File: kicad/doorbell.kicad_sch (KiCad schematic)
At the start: 94 parts, among them J1 USB-C (USB4105), J2 WF26 bus, K1 GAQW212GS, K2 GAQY212GS, K3 GAQY412EH, K4 GAQY412EH, K5 G6K-2F-Y DC12, Q3 2N7002, Q4 2N7002, SW1 BOOT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

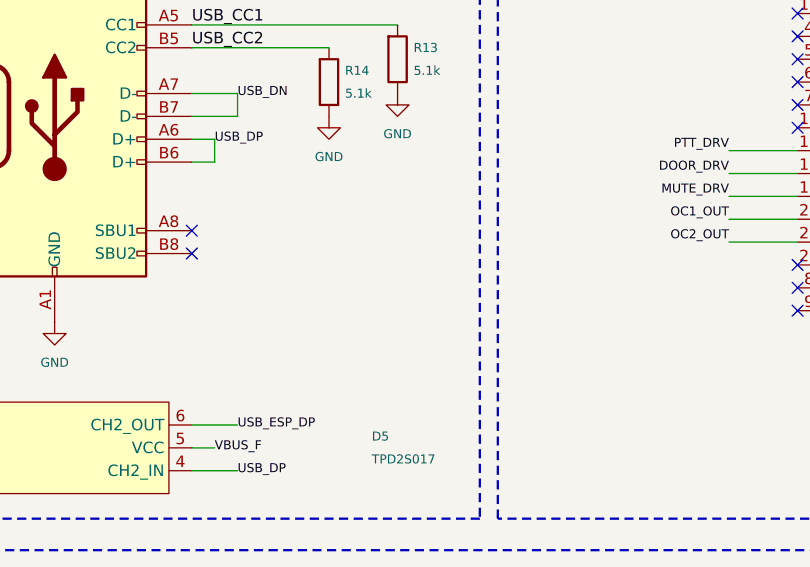
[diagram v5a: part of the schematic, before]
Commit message: kicad+sim: dedicated LP5907 AVDD LDO + J3 USB wall-feed connector
kicad:
- AVDD now comes from a dedicated low-noise LDO (U4 = LP5907MFX-3.3) off +5V:
  AU_3V3 -> FB1 -> AVDD, isolating the codec analog rail from the Wi-Fi/SMPS-noisy
  +3V3 plane (C23/C24 in/out caps; EN tied to +3V3 for sequencing).
- Add J3 -- JST-SH side-entry wall-feed connector (power + native USB); D+/D-
  routed as a pair on B.Cu to the D5/J1 connector-side hub (shares D5's ESD clamp).
- Sourcing fields (LCSC/MPN/Manufacturer) + role Descriptions for U4 and J3;
  correct FB1's role (second LC pole on AU_3V3, no longer "isolates from +3V3").

sim:
- Model the LP5907 as an LDO (Ldo recognises bare IN/OUT pins, not just VIN/VOUT;
  per-part VIN abs-max -- 6 V for the LP5907 vs 22 V for the SGM2212) and register
  it in the model-coverage gate.
- RX tests now drive only the external VBUS, so AVDD comes up through the new LDO.

TODO: defer VBUS source isolation between J1 (USB-C) and J3 (wall feed) --
TPS2116 power-mux or a two-diode front-OR; no board room for it now.
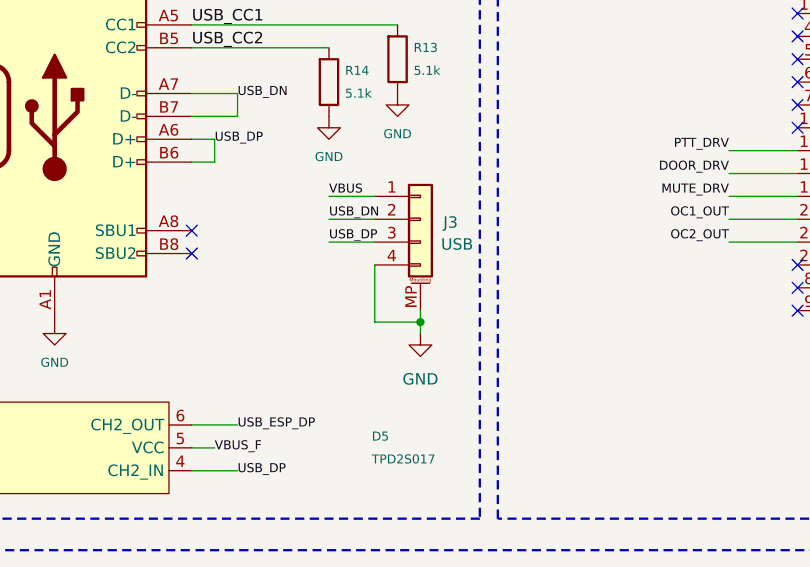
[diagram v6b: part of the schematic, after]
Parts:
- added J3: USB, Connector_JST:JST_SH_SM04B-SRSS-TB_1x04-1MP_P1.00mm_Horizontal, symbol Connector_Generic_MountingPin:Conn_01x04_MountingPin
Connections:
- net GND: now also J3.4 (Pin_4), J3.MP (MountPin)
- net USB_DN: now also J3.2 (Pin_2)
- net USB_DP: now also J3.3 (Pin_3)
- net VBUS: now also J3.1 (Pin_1)

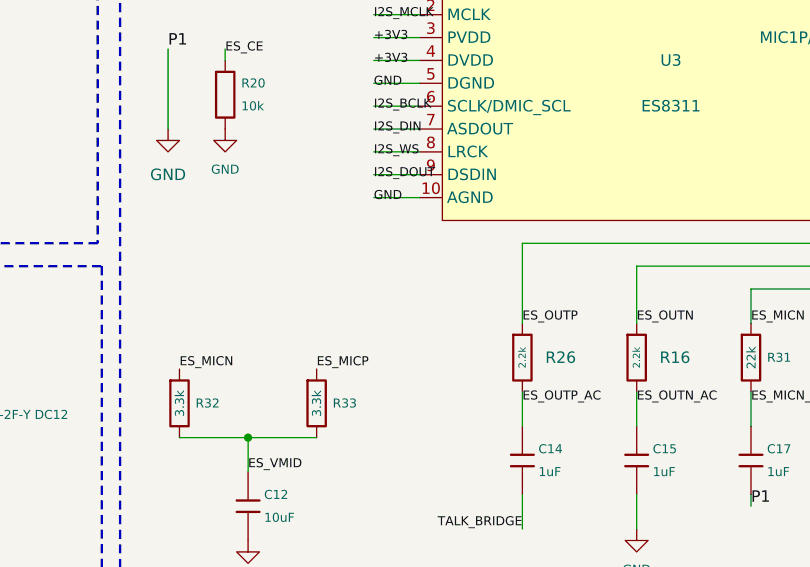
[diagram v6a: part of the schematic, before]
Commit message: codec OUTP clamp (D13 BAT54S) + sim model + doc sync
Add the BAT54S dual-series Schottky clamp at the ES8311 OUTP (D13: COM -> ES_OUTP,
A -> GND, K -> +3V3) as the OUTP abs-max guard. R26 limits the current into it, so the
clamp holds OUTP within [AGND-0.3, AVDD+0.3] against both the per-talk-start K1-make
transient and a single-fault C14-short, instead of leaning on the codec's unrated
internal ESD diode. Board placed + routed, zones refilled, DRC clean.

- sim: DiodeArray model for the 3-pin series array (Diode only handles 2-terminal
  parts) + reviewed model-coverage entry; 50/50 tests pass
- DESIGN.md: TX front-end note -> "R26 + D13 form the OUTP abs-max guard"
- REQUIREMENTS.md: AUDIO-9 (TX/OUTP abs-max, counterpart to AUDIO-8)
- TODO.md: drop completed items (OUTP clamp, SW4 PTT fit, D5 refdes)
- remove stale scratch docs (CODEC_AVDD_REWORK.md, JLCPCB-BASIC-PARTS.md)
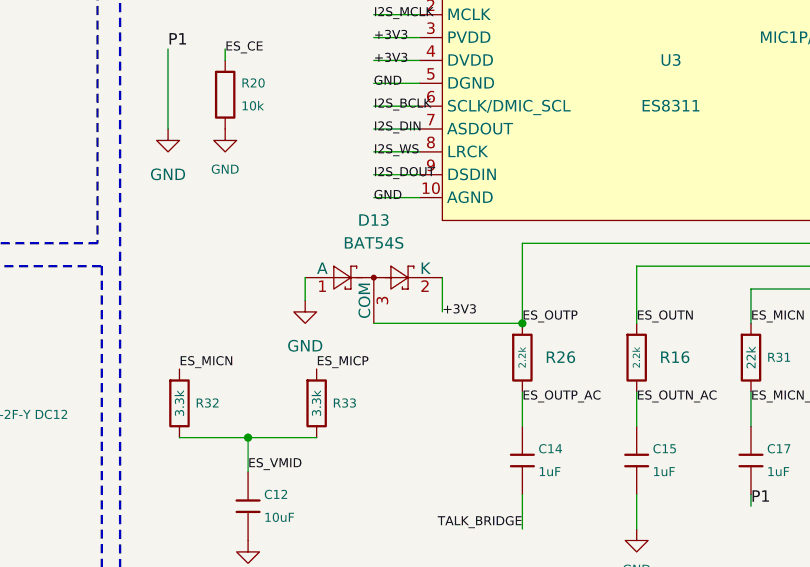
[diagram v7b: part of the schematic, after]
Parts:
- added D13: BAT54S, Package_TO_SOT_SMD:SOT-23, symbol Diode:BAT54S
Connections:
- net +3V3: now also D13.2 (K)
- net ES_OUTP: now also D13.3 (COM)
- net GND: now also D13.1 (A)
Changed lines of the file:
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@@
 	)
 	(junction
+		(at 203.2 217.17)
+		(diameter 0)
+		(color 0 0 0 0)
+	)
+	(junction
 		(at 226.06 29.21)
 		(diameter 0)
@@
 	(wire
 		(pts
+			(xy 186.69 217.17) (xy 203.2 217.17)
+		)
+		(stroke
+			(width 0)
+			(type default)
+		)
+	)
+	(wire
+		(pts
 			(xy 63.5 85.09) (xy 68.58 85.09)
 		)
@@
 	(wire
 		(pts
+			(xy 179.07 212.09) (xy 179.07 214.63)
+		)
+		(stroke
+			(width 0)
+			(type default)
+		)
+	)
+	(wire
+		(pts
 			(xy 43.18 138.43) (xy 49.53 138.43)
 		)
@@
 	(wire
 		(pts
+			(xy 194.31 212.09) (xy 194.31 215.9)
+		)
+		(stroke
+			(width 0)
+			(type default)
+		)
+	)
+	(wire
+		(pts
 			(xy 22.86 251.46) (xy 50.8 251.46)
 		)
@@
 		)
 	)
+	(label "+3V3"
+		(at 194.31 215.9 0)
+		(effects
+			(font
+				(size 1 1)
+			)
+			(justify left)
+		)
+	)
 	(label "DOOR_DRV"
 		(at 285.75 180.34 180)
@@
 			)
 		)
-    (property "LCSC" "C160404" (at 88.9 62.23 0)
-      (effects (font (size 1.27 1.27)) (hide yes))
-    )
-    (property "MPN" "SM04B-SRSS-TB(LF)(SN)" (at 88.9 62.23 0)
-      (effects (font (size 1.27 1.27)) (hide yes))
-    )
-    (property "Manufacturer" "JST" (at 88.9 62.23 0)
-      (effects (font (size 1.27 1.27)) (hide yes))
-    )
+		(property "LCSC" "C160404"
+			(at 88.9 62.23 0)
+			(hide yes)
+			(show_name no)
+			(do_not_autoplace no)
+			(effects
+				(font
+					(size 1.27 1.27)
+				)
+			)
+		)
+		(property "MPN" "SM04B-SRSS-TB(LF)(SN)"
+			(at 88.9 62.23 0)
+			(hide yes)
+			(show_name no)
+			(do_not_autoplace no)
+			(effects
+				(font
+					(size 1.27 1.27)
+				)
+			)
+		)
+		(property "Manufacturer" "JST"
+			(at 88.9 62.23 0)
+			(hide yes)
+			(show_name no)
+			(do_not_autoplace no)
+			(effects
+				(font
+					(size 1.27 1.27)
+				)
+			)
+		)
 		(pin "1"
 		)
@@
 	)
 	(symbol
+		(lib_id "power:GND")
+		(at 179.07 214.63 0)
+		(unit 1)
+		(body_style 1)
+		(exclude_from_sim no)
+		(in_bom yes)
+		(on_board yes)
+		(in_pos_files yes)
+		(dnp no)
+		(fields_autoplaced yes)
+		(property "Reference" "#PWR059"
+			(at 179.07 220.98 0)
+			(hide yes)
+			(show_name no)
+			(do_not_autoplace no)
+			(effects
+				(font
+					(size 1.27 1.27)
+				)
+			)
+		)
+		(property "Value" "GND"
+			(at 179.07 219.71 0)
+			(show_name no)
+			(do_not_autoplace no)
+			(effects
+				(font
+					(size 1.27 1.27)
+				)
+			)
+		)
+		(property "Footprint" ""
+			(at 179.07 214.63 0)
+			(hide yes)
+			(show_name no)
+			(do_not_autoplace no)
+			(effects
+				(font
+					(size 1.27 1.27)
+				)
+			)
+		)
+		(property "Datasheet" ""
+			(at 179.07 214.63 0)
+			(hide yes)
+			(show_name no)
+			(do_not_autoplace no)
+			(effects
+				(font
+					(size 1.27 1.27)
+				)
+			)
+		)
+		(property "Description" "Power symbol creates a global label with name \"GND\" , ground"
+			(at 179.07 214.63 0)
+			(hide yes)
+			(show_name no)
+			(do_not_autoplace no)
+			(effects
+				(font
+					(size 1.27 1.27)
+				)
+			)
+		)
+		(pin "1"
+		)
+		(instances
+			(project "doorbell"
+				(path "/959c5810-086a-4a51-98b0-f68b22907a4f"
+					(reference "#PWR059")
+					(unit 1)
+				)
+			)
+		)
+	)
+	(symbol
 		(lib_id "power:+3V3")
 		(at 146.05 20.32 0)
@@
 					(unit 1)
 				)
+			)
+		)
+	)
+	(symbol
+		(lib_id "Diode:BAT54S")
+		(at 186.69 212.09 0)
+		(unit 1)
+		(body_style 1)
+		(exclude_from_sim no)
+		(in_bom yes)
+		(on_board yes)
+		(in_pos_files yes)
+		(dnp no)
+		(fields_autoplaced yes)
+		(property "Reference" "D13"
+			(at 186.69 205.74 0)
+			(show_name no)
+			(do_not_autoplace no)
+			(effects
+				(font
+					(size 1.27 1.27)
+				)
+			)
+		)
+		(property "Value" "BAT54S"
+			(at 186.69 208.28 0)
+			(show_name no)
+			(do_not_autoplace no)
+			(effects
+				(font
+					(size 1.27 1.27)
+				)
+			)
+		)
+		(property "Footprint" "Package_TO_SOT_SMD:SOT-23"
+			(at 188.595 208.915 0)
+			(hide yes)
+			(show_name no)
+			(do_not_autoplace no)
+			(effects
+				(font
+					(size 1.27 1.27)
+				)
+				(justify left)
+			)
+		)
+		(property "Datasheet" "https://www.diodes.com/assets/Datasheets/ds11005.pdf"
+			(at 183.642 212.09 0)
+			(hide yes)
+			(show_name no)
+			(do_not_autoplace no)
+			(effects
+				(font
+					(size 1.27 1.27)
+				)
+			)
+		)
+		(property "Description" "Vr 30V, If 200mA, Dual schottky barrier diode, in series, SOT-323"
+			(at 186.69 212.09 0)
+			(hide yes)
+			(show_name no)
+			(do_not_autoplace no)
+			(effects
+				(font
+					(size 1.27 1.27)
+				)
+			)
+		)
+		(pin "1"
+		)
+		(pin "2"
+		)
+		(pin "3"
+		)
+		(instances
+			(project "doorbell"
+				(path "/959c5810-086a-4a51-98b0-f68b22907a4f"
+					(reference "D13")
+					(unit 1)
+				)

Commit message: docs + BOM sourcing: D13 LCSC, full datasheet set, MCU/vendor doc fixes
Completes the fab BOM and brings the docs in line with the actual board.

- kicad: set D13 (BAT54S) sourcing -- LCSC C19726 (onsemi BAT54SLT1G), MPN/Mfr,
  onsemi datasheet, corrected description (SOT-23, not SOT-323). This was the last
  thing blocking ./build.sh (the BOM requires an LCSC # per assembled part); the
  full verify + fab run is now clean end-to-end.

- docs: add the 9 missing BOM-part datasheets (BAT54S, Littelfuse 0466 fuse,
  RVT 47uF/50V, 1N4148W, KT-0603R LED, USB4105, DB125, JST SM04B, TS-1088). Every
  assembled part except the generic MLCCs/resistors now has a local sheet.

- docs/attic: relocate 14 superseded datasheets (old C3/C6/S3-MINI MCU variants,
  AMS1117, CP2102N, tantalum study, dropped isolation transformer, alt switch).
  HJR4102 stays in docs/ -- it is WF26 latch-relay reference, not a rejected part.

- docs: correct U1 from ESP32-S3-MINI-1U to ESP32-S3-WROOM-1U-N16R8 across
  ORDERING.md / VERIFICATION.md / ESP32_PCB_BEST_PRACTICES.md / README.md, incl.
  the memory config (N16R8 = 16 MB flash + 8 MB octal PSRAM, not N8/no-PSRAM).
  Verified the N16R8 octal-PSRAM pins (GPIO33-37) are no-connect in the schematic
  -- no pin conflict. Also fix the GAQY412E/EH PhotoMOS vendor label
  (Panasonic -> SUPSiC) in README + VERIFICATION.
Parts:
- D13: LCSC (none) -> C19726; MPN (none) -> BAT54SLT1G; Manufacturer (none) -> onsemi
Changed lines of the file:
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@@
 			)
 		)
-		(property "Datasheet" "https://www.diodes.com/assets/Datasheets/ds11005.pdf"
+		(property "Datasheet" "https://www.lcsc.com/datasheet/lcsc_datasheet_1810301516_onsemi-BAT54SLT1G_C19726.pdf"
 			(at 183.642 212.09 0)
 			(hide yes)
@@
 			)
 		)
-		(property "Description" "Vr 30V, If 200mA, Dual schottky barrier diode, in series, SOT-323"
+		(property "Description" "BAT54S dual-series Schottky (30 V / 200 mA, SOT-23) — codec OUTP abs-max clamp: COM→ES_OUTP, A→GND, K→+3V3"
 			(at 186.69 212.09 0)
 			(hide yes)
@@
 			)
 		)
+    (property "LCSC" "C19726" (at 186.69 212.09 0)
+      (effects (font (size 1.27 1.27)) (hide yes))
+    )
+    (property "MPN" "BAT54SLT1G" (at 186.69 212.09 0)
+      (effects (font (size 1.27 1.27)) (hide yes))
+    )
+    (property "Manufacturer" "onsemi" (at 186.69 212.09 0)
+      (effects (font (size 1.27 1.27)) (hide yes))
+    )
 		(pin "1"
 		)
